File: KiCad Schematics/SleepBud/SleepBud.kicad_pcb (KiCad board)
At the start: 2 copper layers, 165 x 55 mm, 84 parts, among them J1 12V Barrel Jack, J2 USB_B_Micro, J3 Button Connector, J4 AM312 Connector, J5 LED Lamp Connector, J6 Connector to Buzzer, Q1 FQP27P06, Q2 AO3400A, SW1 EN Button, SW2 Reset Button, U1 AMS1117-3.3, U2 AZ1084CD, U3 ESP32-S3-WROOM-1, U4 DS3231SN_, U5 TXS0108EPW

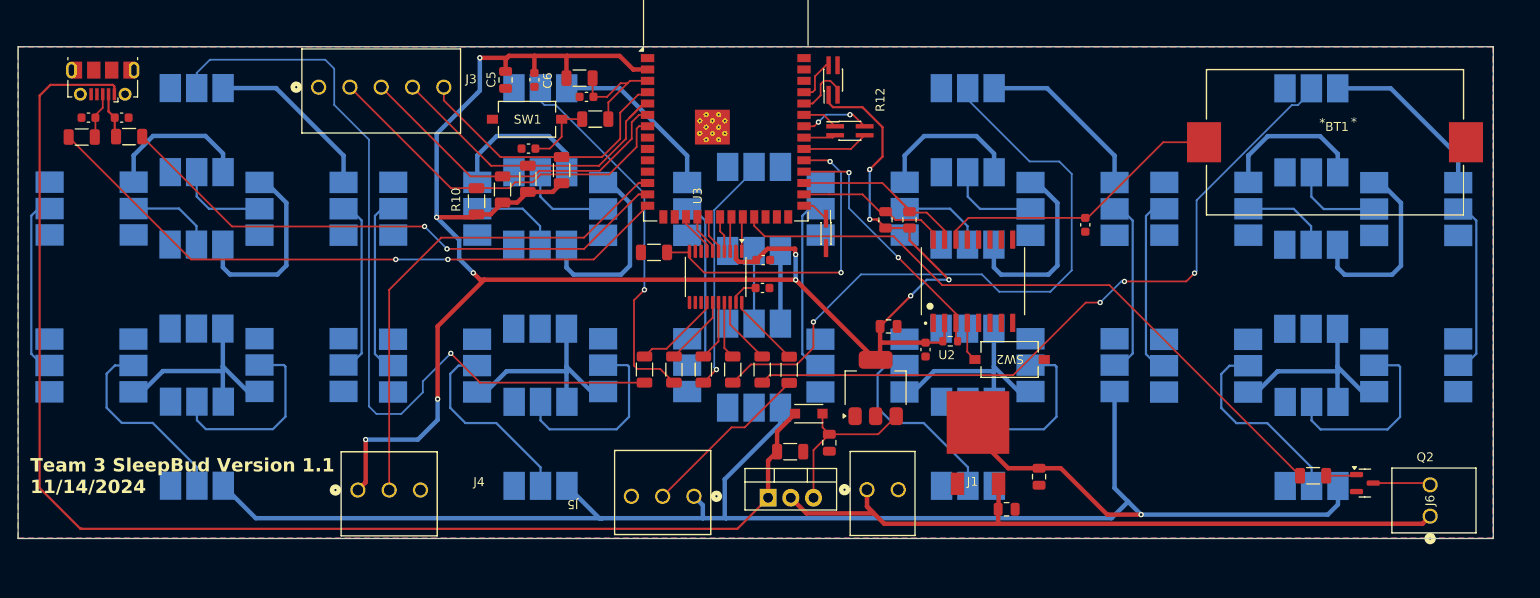
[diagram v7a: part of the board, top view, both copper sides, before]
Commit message: Fixed all violations on PCB
Just need to work on grounding parts, and switching mosfets, adding connections
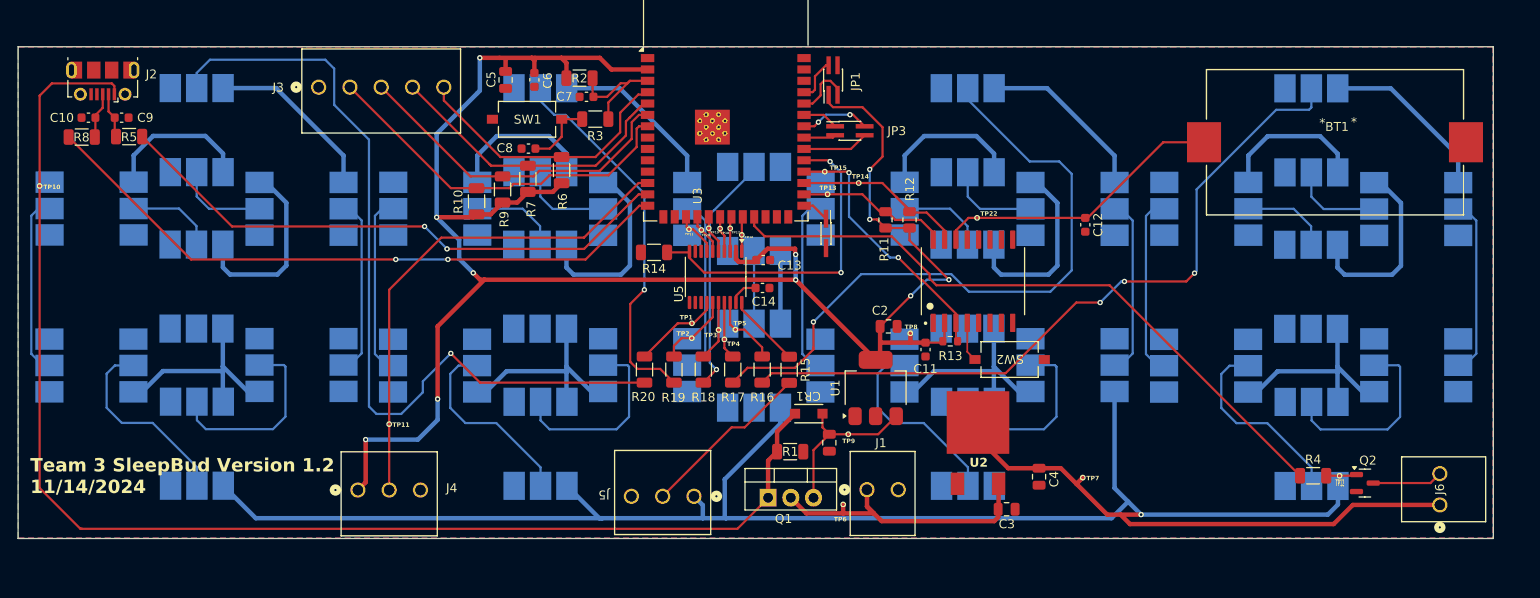
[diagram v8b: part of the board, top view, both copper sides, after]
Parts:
- added TP1: TestPoint_Flag, Custom Pads:Testpoint Pad, F.Cu at (132.6, 87.3)
- added TP10: TestPoint_Flag, Custom Pads:Testpoint Pad, F.Cu at (59.6, 71.9)
- added TP11: TestPoint_Flag, Custom Pads:Testpoint Pad, F.Cu at (98.7, 98.6)
- added TP12: TestPoint_Flag, Custom Pads:Testpoint Pad, F.Cu at (205.0, 104.3)
- added TP13: TestPoint_Flag, Custom Pads:Testpoint Pad, F.Cu at (147.8, 72.8)
- added TP14: TestPoint_Flag, Custom Pads:Testpoint Pad, F.Cu at (151.2, 71.6)
- added TP15: TestPoint_Flag, Custom Pads:Testpoint Pad, F.Cu at (147.4, 70.3)
- added TP16: TestPoint_Small, Custom Pads:Testpoint Pad, F.Cu at (138.2, 77.4)
- added TP17: TestPoint_Small, Custom Pads:Testpoint Pad, F.Cu at (136.9, 76.7)
- added TP18: TestPoint_Small, Custom Pads:Testpoint Pad, F.Cu at (135.7, 76.7)
- added TP19: TestPoint_Small, Custom Pads:Testpoint Pad, F.Cu at (134.5, 76.7)
- added TP2: TestPoint_Flag, Custom Pads:Testpoint Pad, F.Cu at (132.6, 89.0)
- added TP20: TestPoint_Small, Custom Pads:Testpoint Pad, F.Cu at (133.7, 76.8)
- added TP21: TestPoint_Small, Custom Pads:Testpoint Pad, F.Cu at (132.3, 76.8)
- added TP22: TestPoint_Flag, Custom Pads:Testpoint Pad, F.Cu at (164.5, 75.5)
- added TP3: TestPoint_Flag, Custom Pads:Testpoint Pad, F.Cu at (135.6, 88.0)
- added TP4: TestPoint_Flag, Custom Pads:Testpoint Pad, F.Cu at (136.2, 89.1)
- added TP5: TestPoint_Flag, Custom Pads:Testpoint Pad, F.Cu at (137.4, 88.0)
- added TP6: TestPoint_Flag, Custom Pads:Testpoint Pad, F.Cu at (149.5, 107.5)
- added TP7: TestPoint_Flag, Custom Pads:Testpoint Pad, F.Cu at (176.3, 104.5)
- added TP8: TestPoint_Flag, Custom Pads:Testpoint Pad, F.Cu at (157.0, 88.4)
- added TP9: TestPoint_Flag, Custom Pads:Testpoint Pad, F.Cu at (150.1, 99.7)
- moved J6 1.66 mm to (216.1, 105.2)
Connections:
- net /Colon renamed /B4 - Colon
- net /Digit 1 renamed /B2 - Digit 1
- net /Digit 2 renamed /B3 - Digit 2
- net /Digit 3 renamed /B5 - Digit 3
- net /Digit 4 renamed /B6 - Digit 4
- net Net-(U3-IO10) renamed /IO10 - A5
- net Net-(U3-IO11) renamed /IO11 - A4
- net Net-(U3-IO12) renamed /IO12 - A3
- net Net-(U3-IO13) renamed /IO13 - A2
- net Net-(U3-IO14) renamed /IO14 - A1
- net Net-(U3-IO35) renamed /IO35-SCL
- net Net-(U3-IO36) renamed /IO36-SDA
- net Net-(U3-IO37) renamed /IO37-SQW/INT
- net Net-(U3-IO38) renamed /IO38-OE
- net Net-(U3-IO8) renamed /IO8 - Output2
- net Net-(U3-IO9) renamed /IO9 - A6
- J6 pad 1: +12V -> +5V
- U4 pad 10: GND -> (no net)
- U4 pad 11: GND -> (no net)
- U4 pad 12: GND -> (no net)
- U4 pad 5: GND -> (no net)
- U4 pad 6: GND -> (no net)
- U4 pad 7: GND -> (no net)
- U4 pad 8: GND -> (no net)
- U4 pad 9: GND -> (no net)
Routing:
- net +12V: track 81.4 -> 33.3 mm
- net +5V: track 530.2 -> 568.2 mm
- net Net-(D1-DIN): track 80.1 -> 82.2 mm
- net Net-(Q2-D): track 6.45 -> 7.89 mm
- net /B6 - Digit 4: track 9.87 -> 10.6 mm
- net /B5 - Digit 3: track 7.84 -> 8.51 mm
- net /B2 - Digit 1: track 7.52 -> 8.11 mm
- net /IO37-SQW/INT: track 29.1 -> 29.6 mm
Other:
- board text added: "Team 3 SleepBud Version 1.2 11/14/2024"
- board text removed: "Team 3 SleepBud Version 1.1 11/14/2024"
